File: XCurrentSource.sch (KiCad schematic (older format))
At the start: 28 parts, among them Q1 MMBT3906, Q2 MMBT3904, Q3 MMBT3906, Q4 MMBT3904, Q5 MMBT3906, Q6 MMBT3904, Q7 MMBFJ309, U8 LM358

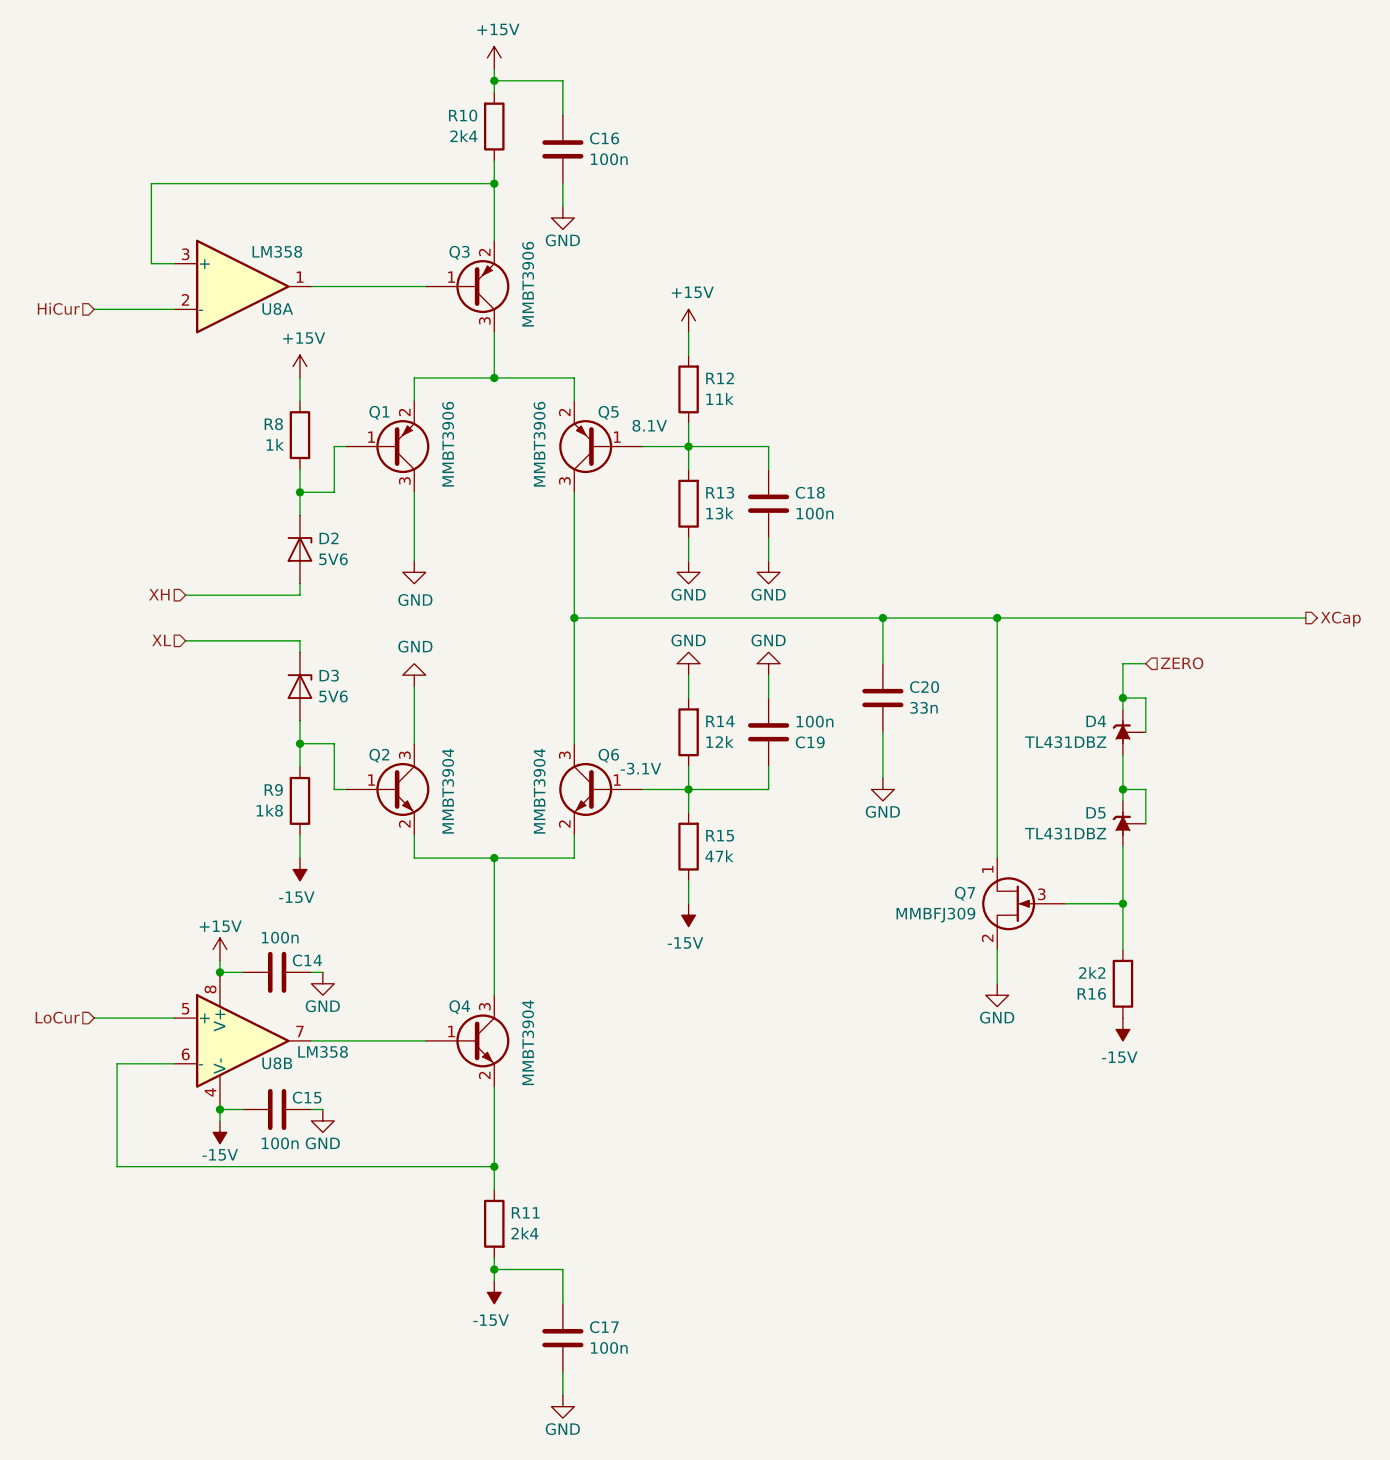
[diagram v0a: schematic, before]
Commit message: Fixed some bugs, finished block symbols
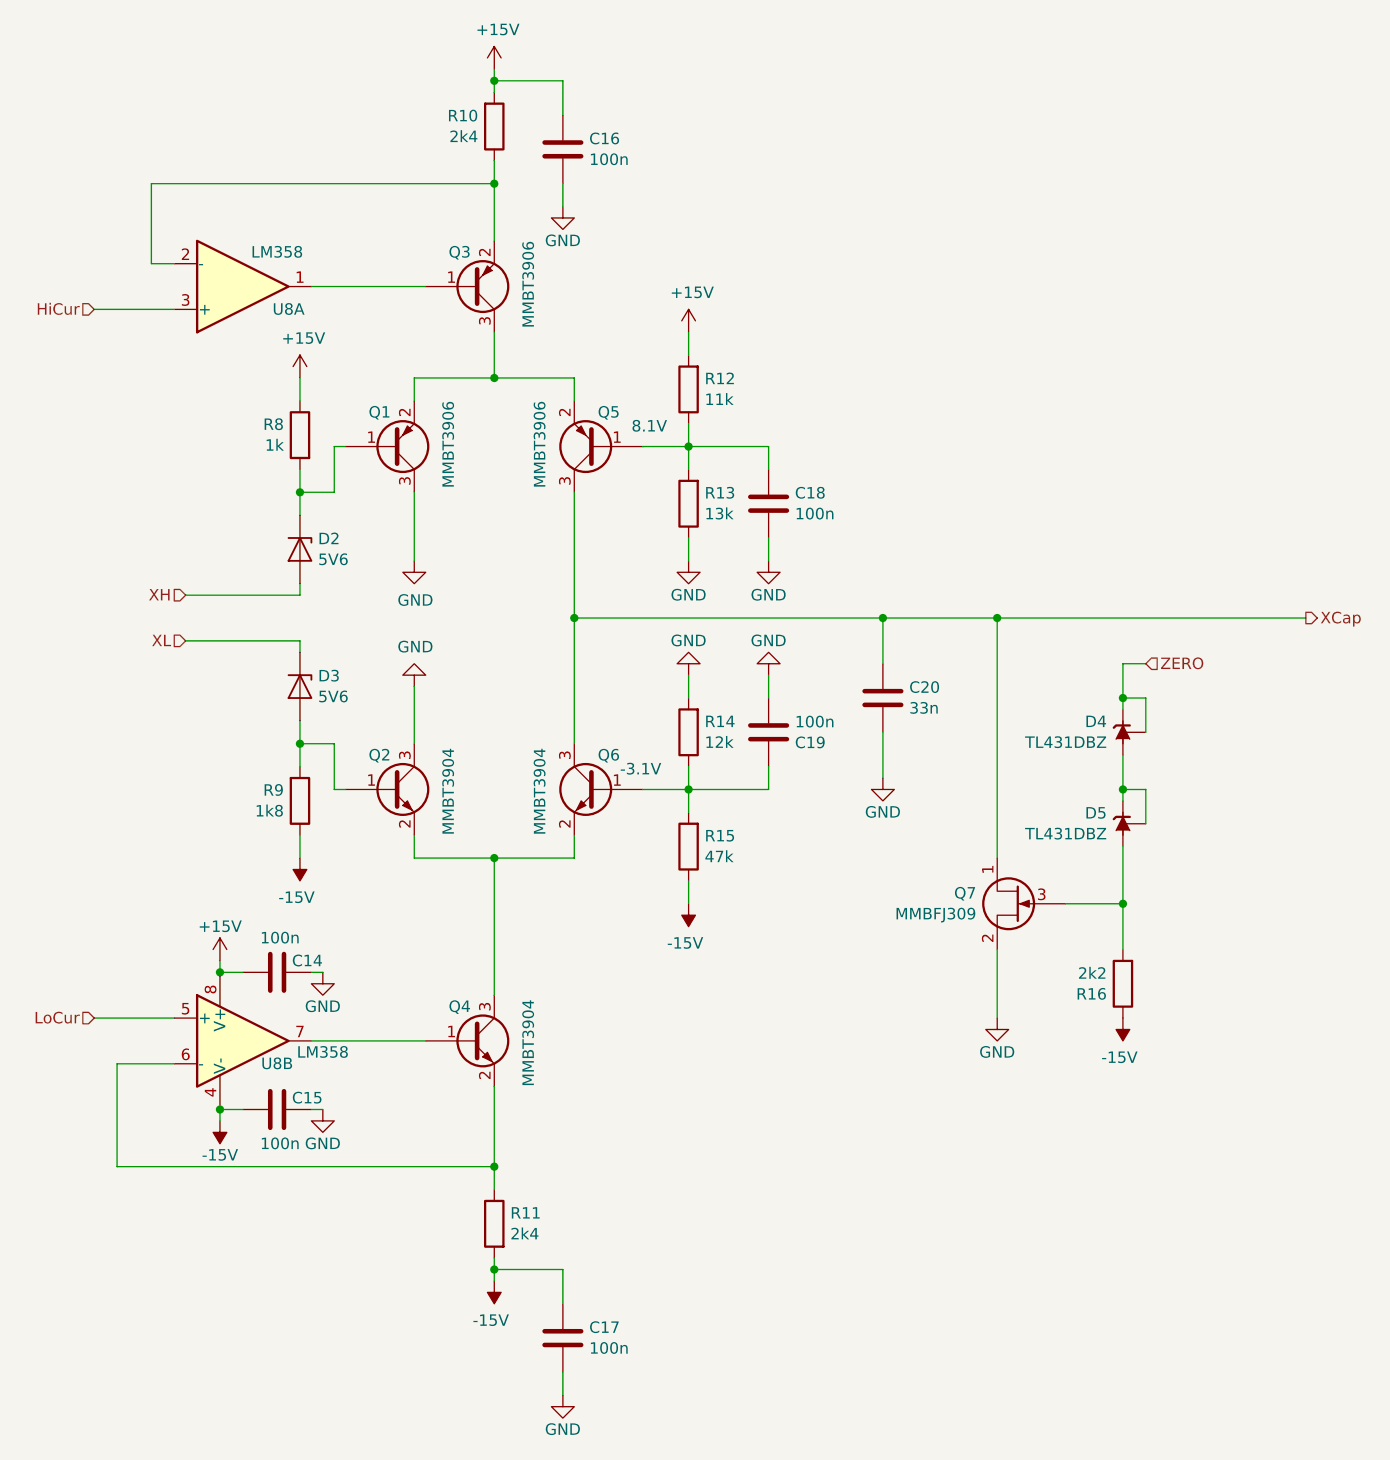
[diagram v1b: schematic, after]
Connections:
- net HiCur: now also U8.3 (+); no longer U8.2 (-)
- net at Q3.2 (E), R10.1: now also U8.2 (-); no longer U8.3 (+)
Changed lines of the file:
@@
 encoding utf-8
 Sheet 7 13
-Title ""
-Date ""
-Rev ""
-Comp ""
-Comment1 ""
+Title "X Current Source"
+Date "2021-04-20"
+Rev "2.0"
+Comp "Filip Piórski"
+Comment1 "Charges/discharges/leaves the signal cap alone"
 Comment2 ""
 Comment3 ""
@@
 AR Path="/601DE80D/60394AE9/604351D8" Ref="U?"  Part="1"
 AR Path="/601E8CCD/604351D8" Ref="U8"  Part="1"
-F 0 "U8" H 3300 2000 50  0000 C CNN
-F 1 "LM358" H 3300 2250 50  0000 C CNN
+F 0 "U8" H 3350 2200 50  0000 C CNN
+F 1 "LM358" H 3300 1950 50  0000 C CNN
 F 2 "Package_SO:SOIC-8_3.9x4.9mm_P1.27mm" H 3150 2100 50  0001 C CNN
 F 3 "http://www.ti.com/lit/ds/symlink/lm2904-n.pdf" H 3150 2100 50  0001 C CNN
 	1    3150 2100
-	1    0    0    -1
+	1    0    0    1
 $EndComp
 $Comp
@@
 L power:GND #PWR?
 U 1 1 602298FE
-P 6450 5150
+P 6450 5300
 AR Path="/5FA4B51C/602298FE" Ref="#PWR?"  Part="1"
 AR Path="/601DE80D/602298FE" Ref="#PWR?"  Part="1"
@@
 AR Path="/601E8CD6/602298FE" Ref="#PWR?"  Part="1"
 AR Path="/601E8CCD/602298FE" Ref="#PWR063"  Part="1"
-F 0 "#PWR063" H 6450 4900 50  0001 C CNN
-F 1 "GND" H 6450 5000 50  0000 C CNN
-F 2 "" H 6450 5150 50  0001 C CNN
-F 3 "" H 6450 5150 50  0001 C CNN
-	1    6450 5150
-	-1   0    0    -1
-$EndComp
-Wire Wire Line
-	6450 5000 6450 5150
+F 0 "#PWR063" H 6450 5050 50  0001 C CNN
+F 1 "GND" H 6450 5150 50  0000 C CNN
+F 2 "" H 6450 5300 50  0001 C CNN
+F 3 "" H 6450 5300 50  0001 C CNN
+	1    6450 5300
+	-1   0    0    -1
+$EndComp
+Wire Wire Line
+	6450 5000 6450 5300
 Wire Wire Line
 	7000 3750 7100 3750
